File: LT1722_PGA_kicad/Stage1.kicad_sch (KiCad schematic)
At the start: 10 parts, among them U1 LT1722

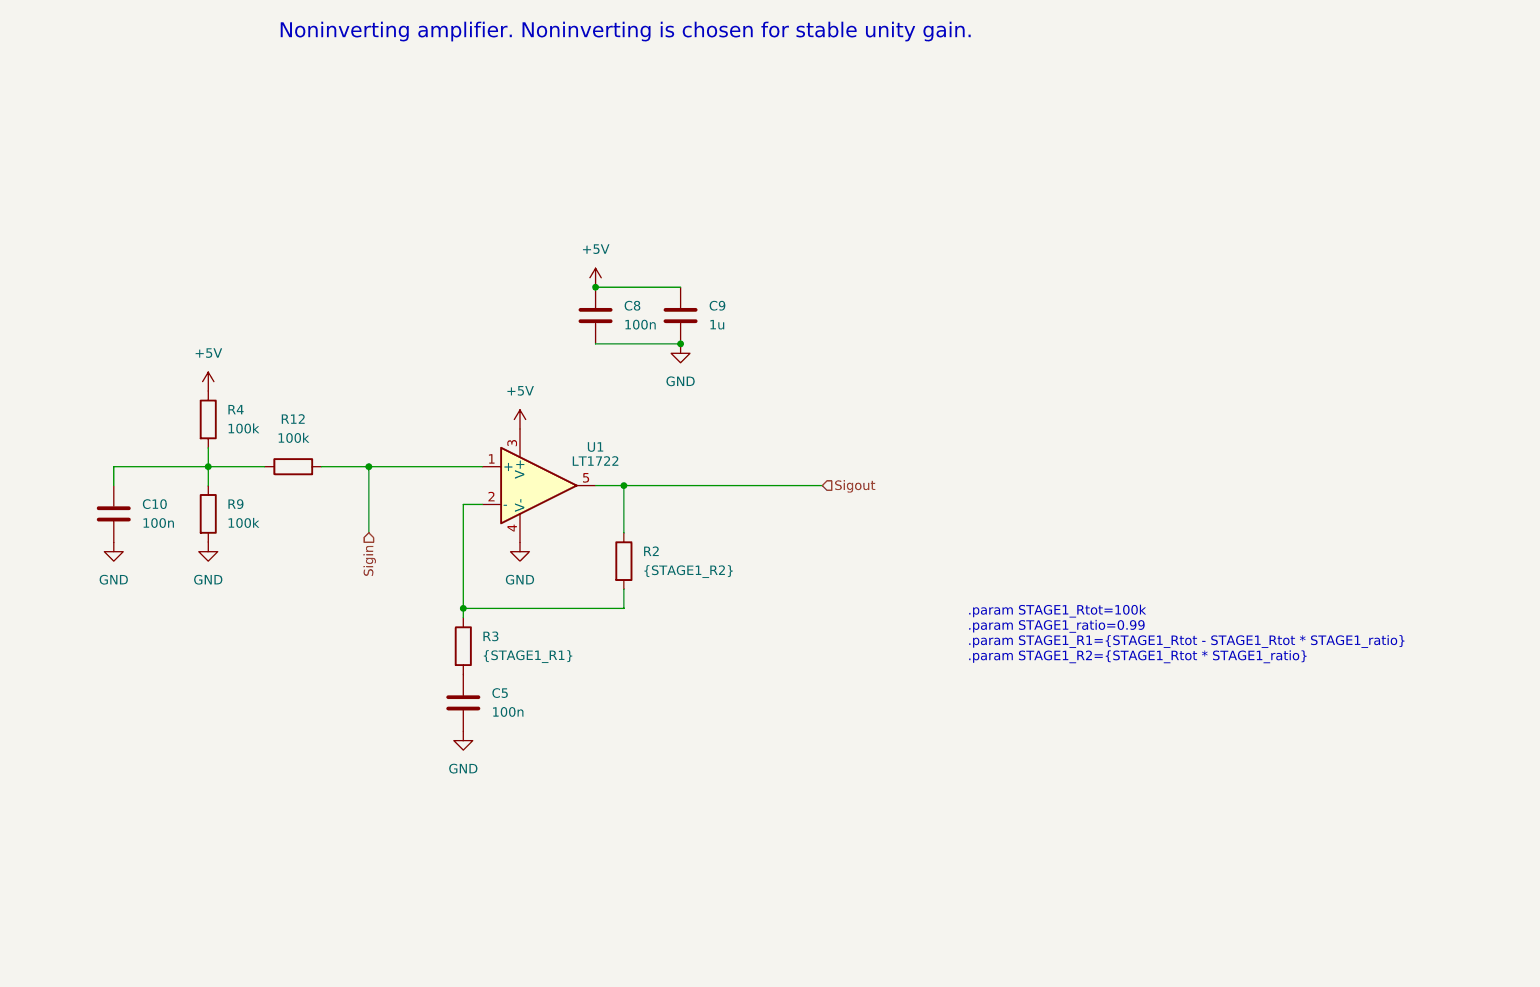
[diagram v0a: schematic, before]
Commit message: change stage1 and pga to be tuned
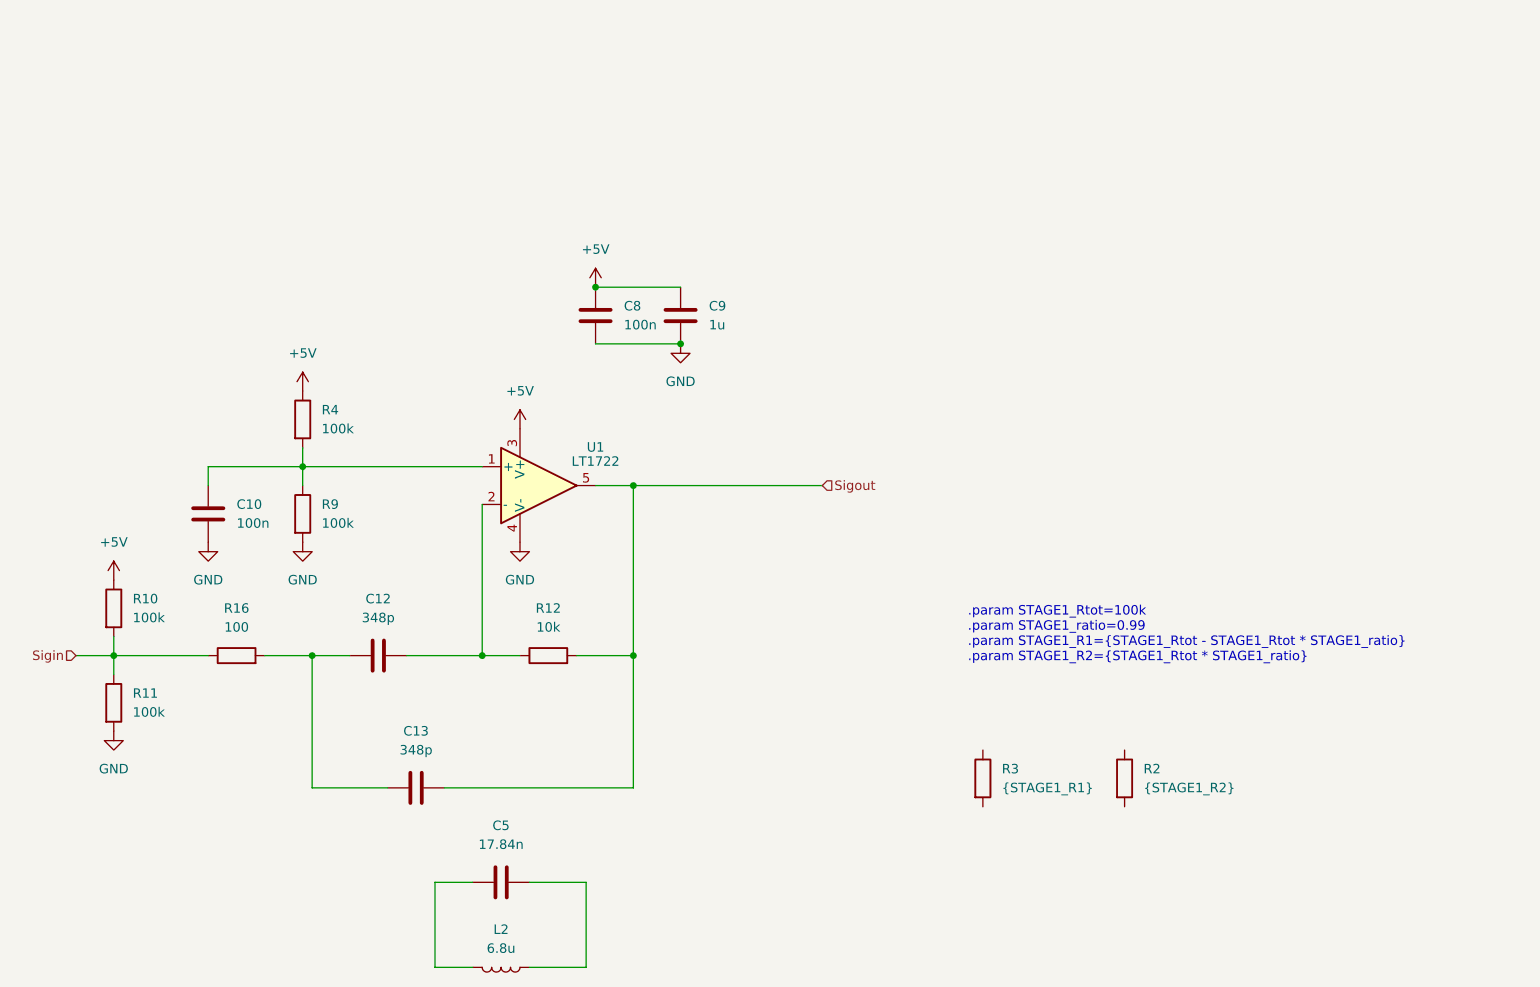
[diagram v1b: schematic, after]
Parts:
- added C12, C13: 348p, symbol Device:C
- added L2: 6.8u, symbol Device:L
- added R10, R11: 100k, symbol Device:R
- added R16: 100, symbol Device:R
- C5: value 100n -> 17.84n
- R12: value 100k -> 10k
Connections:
- net +5V: now also R10.1
- net GND: now also R11.2; no longer C5.2
- net Sigin: now also R10.2, R11.1, R16.1; no longer R12.2, U1.1 (+)
- net Sigout: now also R12.2, C13.2; no longer R2.1
- net at R3.2: no longer C5.1
- net at C10.1, R4.2, R9.1: now also U1.1 (+); no longer R12.1
- new net: C12.2, R12.1, U1.2 (-)
- new net: C12.1, C13.1, R16.2
- new net: C5.1, L2.2
- new net: C5.2, L2.1
- now unconnected: R2.2, R3.1
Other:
- note removed: "Noninverting amplifier. Noninverting is chosen for stable unity gain."
- moved on the sheet: C10, R2, R3, R4, R9
